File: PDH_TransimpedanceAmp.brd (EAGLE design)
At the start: 19.1 x 25.4 mm, 21 parts, among them U1 LMH6626, X1 UMC, X2 UMC

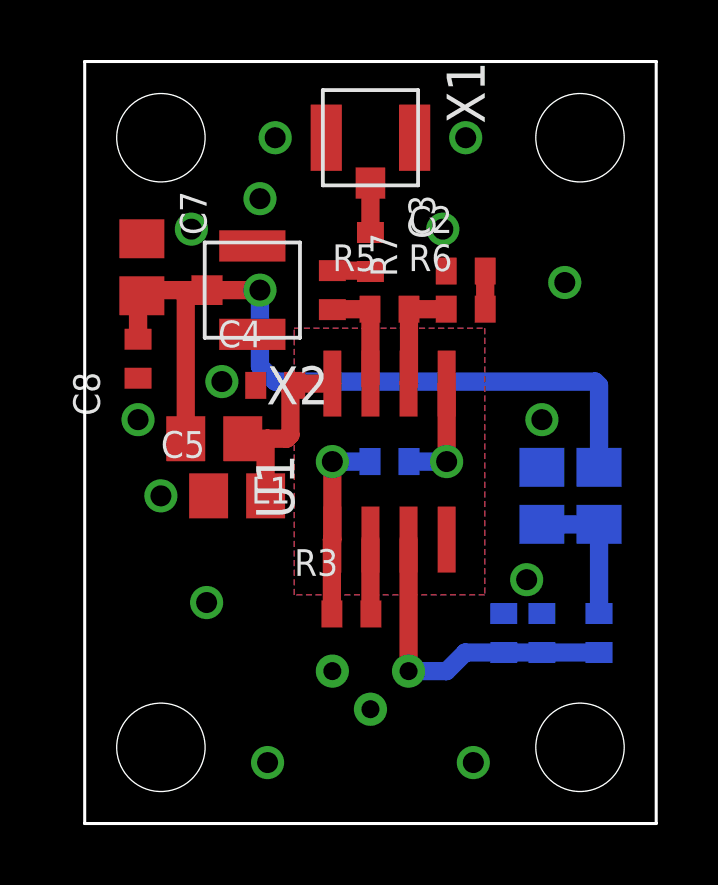
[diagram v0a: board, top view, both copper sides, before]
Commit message: Fixed PD net connection; added BW limiting capacitor
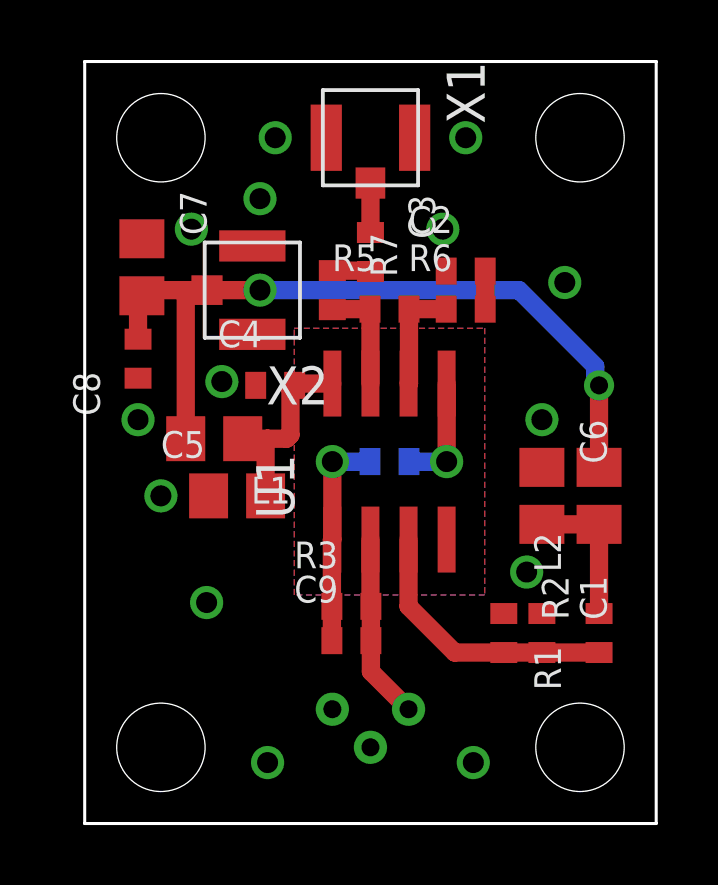
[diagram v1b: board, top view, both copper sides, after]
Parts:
- added C9: (no value), rlc-jqi:0402
- moved D1 1.27 mm to (9.53, 3.81)
- moved R3 0.25 mm to (8.89, 7.24)
- flipped C1 to the top
- flipped C6 to the top
- flipped L2 to the top
- flipped R1 to the top
- flipped R2 to the top
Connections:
- net N$1: no longer D1.P$1
- net N$4: now also C9.2, D1.P$1
- net N$5: now also C9.1
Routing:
- net N$4: track 2.49 -> 6.44 mm
- net N$1: track 11.0 -> 9.21 mm
- net V+: track 27.6 -> 26.5 mm, vias 1 -> 2
- net N$5: track 6.35 -> 7.24 mm
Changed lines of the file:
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@@
 <?xml version="1.0" encoding="utf-8"?>
 <!DOCTYPE eagle SYSTEM "eagle.dtd">
-<eagle version="6.5.0">
+<eagle version="6.2">
 <drawing>
 <settings>
@@
 </class>
 </classes>
-<designrules name="default">
+<designrules>
 <description language="de">&lt;b&gt;EAGLE Design Rules&lt;/b&gt;
 &lt;p&gt;
@@
 <elements>
 <element name="U1" library="RF_TransimpedanceAmp" package="SO08" value="LMH6626" x="9.525" y="12.065" rot="R90"/>
-<element name="R1" library="rlc-jqi" package="0402" value="" x="17.145" y="6.35" rot="MR90"/>
-<element name="R2" library="rlc-jqi" package="0402" value="" x="13.97" y="6.35" rot="MR270"/>
-<element name="C1" library="rlc-jqi" package="0402" value="" x="15.24" y="6.35" rot="MR270"/>
-<element name="R3" library="rlc-jqi" package="0402" value="" x="8.89" y="6.985"/>
+<element name="R1" library="rlc-jqi" package="0402" value="" x="17.145" y="6.35" rot="R90"/>
+<element name="R2" library="rlc-jqi" package="0402" value="" x="13.97" y="6.35" rot="R270"/>
+<element name="C1" library="rlc-jqi" package="0402" value="" x="15.24" y="6.35" rot="R270"/>
+<element name="R3" library="rlc-jqi" package="0402" value="" x="8.89" y="7.239"/>
 <element name="R4" library="rlc-jqi" package="0402" value="" x="10.16" y="12.065" rot="MR0"/>
 <element name="R5" library="rlc-jqi" package="0402" value="" x="10.16" y="17.145"/>
@@
 <element name="C5" library="rlc-jqi" package="0805" value="" x="5.08" y="10.922"/>
 <element name="L1" library="rlc-jqi" package="0805" value="Ferrite" x="4.318" y="12.827" rot="R180"/>
-<element name="L2" library="rlc-jqi" package="0805" value="Ferrite" x="17.145" y="10.922" rot="MR90"/>
-<element name="C6" library="rlc-jqi" package="0805" value="" x="15.24" y="10.922" rot="MR270"/>
-<element name="D1" library="RF_TransimpedanceAmp" package="S5971-CASE" value="S5971" x="9.525" y="5.08" rot="MR180"/>
+<element name="L2" library="rlc-jqi" package="0805" value="Ferrite" x="17.145" y="10.922" rot="R90"/>
+<element name="C6" library="rlc-jqi" package="0805" value="" x="15.24" y="10.922" rot="R270"/>
+<element name="D1" library="RF_TransimpedanceAmp" package="S5971-CASE" value="S5971" x="9.525" y="3.81" rot="MR180"/>
 <element name="X1" library="connector-jqi" package="UMC" value="UMC" x="9.525" y="22.86" rot="R270"/>
 <element name="X2" library="connector-jqi" package="UMC" value="UMC" x="5.588" y="17.78" rot="R180"/>
 <element name="C7" library="rlc-jqi" package="0805" value="" x="1.905" y="18.542" rot="R270"/>
 <element name="C8" library="rlc-jqi" package="0402" value="" x="1.778" y="15.494" rot="R90"/>
+<element name="C9" library="rlc-jqi" package="0402" value="" x="8.89" y="6.096"/>
 </elements>
 <signals>
@@
 <contactref element="U1" pad="3"/>
 <contactref element="C1" pad="2"/>
-<contactref element="D1" pad="P$1"/>
-<wire x1="17.145" y1="5.7" x2="15.24" y2="5.7" width="0.6096" layer="16"/>
-<wire x1="15.24" y1="5.7" x2="13.97" y2="5.7" width="0.6096" layer="16"/>
-<wire x1="10.795" y1="5.065" x2="10.795" y2="5.08" width="0.6096" layer="16"/>
-<wire x1="10.795" y1="9.465" x2="10.795" y2="5.08" width="0.6096" layer="1"/>
-<wire x1="13.97" y1="5.7" x2="12.685" y2="5.7" width="0.6096" layer="16"/>
-<wire x1="12.685" y1="5.7" x2="12.065" y2="5.08" width="0.6096" layer="16"/>
-<wire x1="12.065" y1="5.08" x2="10.795" y2="5.08" width="0.6096" layer="16"/>
+<wire x1="17.145" y1="5.7" x2="15.24" y2="5.7" width="0.6096" layer="1"/>
+<wire x1="15.24" y1="5.7" x2="13.97" y2="5.7" width="0.6096" layer="1"/>
+<wire x1="13.97" y1="5.7" x2="12.334" y2="5.7" width="0.6096" layer="1"/>
+<wire x1="12.334" y1="5.7" x2="10.795" y2="7.239" width="0.6096" layer="1"/>
+<wire x1="10.795" y1="9.465" x2="10.795" y2="7.239" width="0.6096" layer="1"/>
 </signal>
 <signal name="GND" airwireshidden="yes">
@@
 <via x="4.064" y="7.366" extent="1-16" drill="0.7"/>
 <via x="15.24" y="13.462" extent="1-16" drill="0.7"/>
-<via x="14.732" y="8.128" extent="1-16" drill="0.7"/>
+<via x="14.732" y="8.382" extent="1-16" drill="0.7"/>
 <via x="12.954" y="2.032" extent="1-16" drill="0.7"/>
 <via x="16.002" y="18.034" extent="1-16" drill="0.7"/>
@@
 <via x="3.556" y="19.812" extent="1-16" drill="0.7"/>
 <via x="6.096" y="2.032" extent="1-16" drill="0.7"/>
-<wire x1="14.732" y1="8.128" x2="12.065" y2="9.465" width="0" layer="19" extent="1-1"/>
+<wire x1="14.732" y1="8.382" x2="12.065" y2="9.465" width="0" layer="19" extent="1-1"/>
 </signal>
 <signal name="N$4">
 <contactref element="U1" pad="2"/>
 <contactref element="R3" pad="2"/>
-<wire x1="9.54" y1="6.985" x2="9.525" y2="6.985" width="0.6096" layer="1"/>
+<wire x1="9.54" y1="7.239" x2="9.525" y2="6.985" width="0.6096" layer="1"/>
 <wire x1="9.525" y1="6.985" x2="9.525" y2="9.465" width="0.6096" layer="1"/>
+<contactref element="D1" pad="P$1"/>
+<contactref element="C9" pad="2"/>
+<wire x1="9.525" y1="6.985" x2="9.54" y2="6.985" width="0.6096" layer="1"/>
+<wire x1="9.54" y1="6.985" x2="9.54" y2="6.096" width="0.6096" layer="1"/>
+<wire x1="10.795" y1="3.81" x2="9.54" y2="5.065" width="0.6096" layer="1"/>
+<wire x1="9.54" y1="5.065" x2="9.54" y2="6.096" width="0.6096" layer="1"/>
 </signal>
 <signal name="N$5">
@@
 <contactref element="R4" pad="2"/>
 <wire x1="8.255" y1="9.465" x2="8.24" y2="9.465" width="0.6096" layer="1"/>
-<wire x1="8.24" y1="9.465" x2="8.24" y2="6.985" width="0.6096" layer="1"/>
+<wire x1="8.24" y1="9.465" x2="8.24" y2="7.239" width="0.6096" layer="1"/>
 <wire x1="8.255" y1="9.465" x2="8.255" y2="12.065" width="0.6096" layer="1"/>
 <via x="8.255" y="12.065" extent="1-16" drill="0.7"/>
 <wire x1="8.255" y1="12.065" x2="9.51" y2="12.065" width="0.6096" layer="16"/>
+<contactref element="C9" pad="1"/>
+<wire x1="8.24" y1="6.096" x2="8.24" y2="7.239" width="0.6096" layer="1"/>
 </signal>
 <signal name="N$6">
@@
 <contactref element="C6" pad="2"/>
 <contactref element="L2" pad="1"/>
-<wire x1="17.145" y1="7" x2="17.145" y2="9.972" width="0.6096" layer="16"/>
-<wire x1="17.145" y1="9.972" x2="15.24" y2="9.972" width="0.6096" layer="16"/>
+<wire x1="17.145" y1="9.972" x2="15.24" y2="9.972" width="0.6096" layer="1"/>
+<wire x1="17.145" y1="9.972" x2="17.145" y2="7" width="0.6096" layer="1"/>
 </signal>
 <signal name="V+">
@@
 <wire x1="3.368" y1="12.827" x2="3.368" y2="17.714" width="0.6096" layer="1"/>
 <wire x1="3.368" y1="17.714" x2="3.302" y2="17.78" width="0.6096" layer="1"/>
-<wire x1="17.145" y1="11.872" x2="17.145" y2="14.605" width="0.6096" layer="16"/>
 <wire x1="17.145" y1="14.605" x2="17.018" y2="14.732" width="0.6096" layer="16"/>
-<wire x1="17.018" y1="14.732" x2="6.35" y2="14.732" width="0.6096" layer="16"/>
-<wire x1="6.35" y1="14.732" x2="5.842" y2="15.24" width="0.6096" layer="16"/>
-<wire x1="5.842" y1="15.24" x2="5.842" y2="17.78" width="0.6096" layer="16"/>
 <via x="5.842" y="17.78" extent="1-16" drill="0.7"/>
 <wire x1="5.842" y1="17.78" x2="4.0767" y2="17.78" width="0.6096" layer="1"/>
+<via x="17.145" y="14.605" extent="1-16" drill="0.6"/>
+<wire x1="17.145" y1="14.605" x2="17.145" y2="11.872" width="0.6096" layer="1"/>
+<wire x1="17.018" y1="14.732" x2="17.018" y2="15.24" width="0.6096" layer="16"/>
+<wire x1="17.018" y1="15.24" x2="14.478" y2="17.78" width="0.6096" layer="16"/>
+<wire x1="14.478" y1="17.78" x2="5.842" y2="17.78" width="0.6096" layer="16"/>
 </signal>
 <signal name="N$11">
